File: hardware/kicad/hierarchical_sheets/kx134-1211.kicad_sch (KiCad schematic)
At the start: 0 parts

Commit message: created microcontroller schematic
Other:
- company: (none) -> Missouri S&T Rocket Design Team
- title: (none) -> SRAD-FC
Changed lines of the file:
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@@
 (kicad_sch (version 20230121) (generator eeschema)
-  (paper "A4")
+  (paper "USLetter")
+  (title_block
+    (title "SRAD-FC")
+    (company "Missouri S&T Rocket Design Team")
+  )
 )

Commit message: fixed weird fork on high g accel sheet
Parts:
- added C6, C7: 100n, symbol Device:C
- added U4: KX134-1211, Package_LGA:LGA-12_2x2mm_P0.5mm, symbol Sensor_Motion:KX122-1042
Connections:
- new net +3.3V: C6.1, C7.1, U4.3 (IO_VDD), U4.7 (VDD)
- new net GND: C6.2, C7.2, U4.8 (GND), U4.9 (GND)
- new net MISO: U4.1 (SDO/ADDR)
- new net MOSI: U4.2 (SDI/SDA)
- new net SCK: U4.12 (SCLK/SCL)
- new net ~{CS}: U4.10 (~{nCS})
- no-connect marks 0 -> 4

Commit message: massive comment upload
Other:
- note added: "Comments: - Add a ~{CS} pullup resistor between the ~{CS} pin and 3.3v. Make this resistor 10k. The only purpose of this resistor is to ensure that the chip stays inactive while the microcontroller is being initially programmed since during programming the chip will be unable to hold the various ~{CS} lines high. (The MOSI/MISO lines are used by the programmer so if this chip starts communicating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"
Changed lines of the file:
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@@
     (stroke (width 0) (type default))
+  )
+  (text "Comments:\n\n- Add a ~{CS} pullup resistor between the ~{CS} pin and 3.3v. Make this resistor\n	10k. The only purpose of this resistor is to ensure that the chip stays inactive \n	while the microcontroller is being initially programmed since during programming the chip\n	will be unable to hold the various ~{CS} lines high. (The MOSI/MISO lines \n	are used by the programmer so if this chip starts communicating while\n	the programmer is communicating to the microcontroller it could be really \n	bad.) A higher value resistor is less likely to cause problems during normal \n	operation. \n\n\n			-Seth"
+    (at 113.665 60.96 0)
+    (effects (font (size 2 2) (thickness 0.4) bold (color 255 48 0 1)) (justify left bottom))
   )
   (label "~{CS}" (at 50.8 82.55 0) (fields_autoplaced)

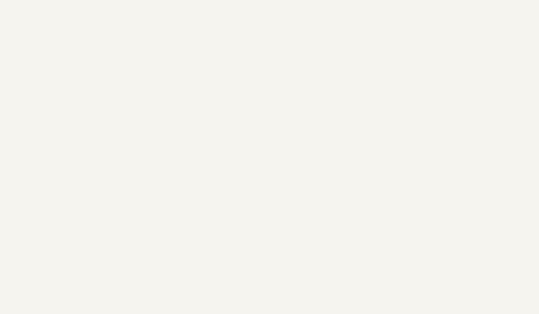
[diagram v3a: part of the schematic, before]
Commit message: added max current
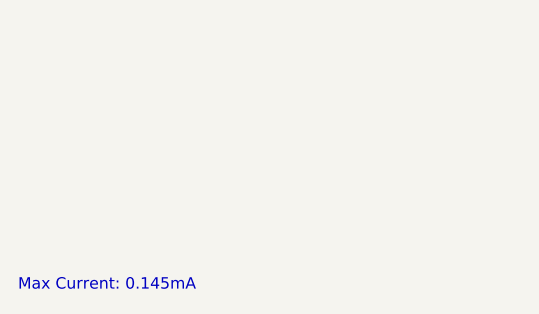
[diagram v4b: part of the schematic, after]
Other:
- note added: "Max Current: 0.145mA"
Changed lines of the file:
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@@
     (effects (font (size 2 2) (thickness 0.4) bold (color 255 48 0 1)) (justify left bottom))
+  )
+  (text "Max Current: 0.145mA" (at 13.97 201.295 0)
+    (effects (font (size 1.27 1.27)) (justify left bottom))
   )
   (label "~{CS}" (at 50.8 82.55 0) (fields_autoplaced)

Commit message: fixed schematic
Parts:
- added R23: 10k, symbol Device:R
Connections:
- net +3.3V: now also R23.1
- net ~{CS}: now also R23.2
- net INT: now reaches U4.5 (INT1)
- no-connect marks 4 -> 3
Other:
- note removed: "Comments: - Add a ~{CS} pullup resistor between the ~{CS} pin and 3.3v. Make this resistor 10k. The only purpose of this resistor is to ensure that the chip stays inactive while the microcontroller is being initially programmed since during programming the chip will be unable to hold the various ~{CS} lines high. (The MOSI/MISO lines are used by the programmer so if this chip starts communicating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"
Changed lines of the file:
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@@
   (junction (at 90.17 52.07) (diameter 0) (color 0 0 0 0)
+  )
+  (junction (at 49.53 82.55) (diameter 0) (color 0 0 0 0)
   )
   (junction (at 90.17 66.04) (diameter 0) (color 0 0 0 0)
@@
   (no_connect (at 80.01 95.25))
   (no_connect (at 80.01 87.63))
-  (no_connect (at 80.01 85.09))
   (wire (pts (xy 90.17 62.23) (xy 90.17 66.04))
+    (stroke (width 0) (type default))
+  )
+  (wire (pts (xy 49.53 82.55) (xy 49.53 76.2))
     (stroke (width 0) (type default))
   )
@@
     (stroke (width 0) (type default))
   )
-  (wire (pts (xy 67.31 74.93) (xy 67.31 67.31))
+  (wire (pts (xy 49.53 63.5) (xy 49.53 68.58))
     (stroke (width 0) (type default))
   )
-  (wire (pts (xy 45.72 82.55) (xy 57.15 82.55))
+  (wire (pts (xy 67.31 74.93) (xy 67.31 67.31))
     (stroke (width 0) (type default))
   )
@@
   )
   (wire (pts (xy 69.85 74.93) (xy 69.85 67.31))
+    (stroke (width 0) (type default))
+  )
+  (wire (pts (xy 49.53 82.55) (xy 57.15 82.55))
+    (stroke (width 0) (type default))
+  )
+  (wire (pts (xy 40.64 82.55) (xy 49.53 82.55))
     (stroke (width 0) (type default))
   )
@@
     (stroke (width 0) (type default))
   )
+  (wire (pts (xy 80.01 85.09) (xy 88.9 85.09))
+    (stroke (width 0) (type default))
+  )
   (wire (pts (xy 90.17 52.07) (xy 90.17 54.61))
     (stroke (width 0) (type default))
@@
     (stroke (width 0) (type default))
   )
-  (text "Comments:\n\n- Add a ~{CS} pullup resistor between the ~{CS} pin and 3.3v. Make this resistor\n	10k. The only purpose of this resistor is to ensure that the chip stays inactive \n	while the microcontroller is being initially programmed since during programming the chip\n	will be unable to hold the various ~{CS} lines high. (The MOSI/MISO lines \n	are used by the programmer so if this chip starts communicating while\n	the programmer is communicating to the microcontroller it could be really \n	bad.) A higher value resistor is less likely to cause problems during normal \n	operation. \n\n\n			-Seth"
-    (at 113.665 60.96 0)
-    (effects (font (size 2 2) (thickness 0.4) bold (color 255 48 0 1)) (justify left bottom))
-  )
   (text "Max Current: 0.145mA" (at 13.97 201.295 0)
     (effects (font (size 1.27 1.27)) (justify left bottom))
   )
-  (label "~{CS}" (at 50.8 82.55 0) (fields_autoplaced)
+  (label "~{CS}" (at 44.45 82.55 0) (fields_autoplaced)
+    (effects (font (size 1.27 1.27)) (justify left bottom))
+  )
+  (label "INT" (at 81.28 85.09 0) (fields_autoplaced)
     (effects (font (size 1.27 1.27)) (justify left bottom))
   )
@@
     (effects (font (size 1.27 1.27)) (justify left bottom))
   )
-  (hierarchical_label "~{CS}" (shape output) (at 45.72 82.55 180) (fields_autoplaced)
+  (hierarchical_label "~{CS}" (shape output) (at 40.64 82.55 180) (fields_autoplaced)
     (effects (font (size 1.27 1.27)) (justify right))
   )
   (hierarchical_label "MISO" (shape output) (at 45.72 87.63 180) (fields_autoplaced)
     (effects (font (size 1.27 1.27)) (justify right))
+  )
+  (hierarchical_label "INT" (shape output) (at 88.9 85.09 0) (fields_autoplaced)
+    (effects (font (size 1.27 1.27)) (justify left))
   )
   (hierarchical_label "MOSI" (shape input) (at 45.72 85.09 180) (fields_autoplaced)
@@
         )
       )
+    )
+  )
+  (symbol (lib_id "Device:R") (at 49.53 72.39 0) (unit 1)
+    (in_bom yes) (on_board yes) (dnp no) (fields_autoplaced)
+    (property "Reference" "R23" (at 52.07 71.12 0)
+      (effects (font (size 1.27 1.27)) (justify left))
+    )
+    (property "Value" "10k" (at 52.07 73.66 0)
+      (effects (font (size 1.27 1.27)) (justify left))
+    )
+    (property "Footprint" "" (at 47.752 72.39 90)
+      (effects (font (size 1.27 1.27)) hide)
+    )
+    (property "Datasheet" "~" (at 49.53 72.39 0)
+      (effects (font (size 1.27 1.27)) hide)
+    )
+    (pin "1")
+    (pin "2")
+    (instances
+      (project "FC"
+        (path "/54cce219-8b98-4e71-96c4-f9ee784aa3bc/cf41b566-7189-40a2-a24f-d689fa8a8692"
+          (reference "R23") (unit 1)
+        )
+      )
+    )
+  )
+  (symbol (lib_id "power:+3.3V") (at 49.53 63.5 0) (unit 1)
+    (in_bom yes) (on_board yes) (dnp no) (fields_autoplaced)
+    (property "Reference" "#PWR042" (at 49.53 67.31 0)
+      (effects (font (size 1.27 1.27)) hide)
+    )
+    (property "Value" "+3.3V" (at 49.53 58.42 0)
+      (effects (font (size 1.27 1.27)))
+    )
+    (property "Footprint" "" (at 49.53 63.5 0)
+      (effects (font (size 1.27 1.27)) hide)
+    )
+    (property "Datasheet" "" (at 49.53 63.5 0)
+      (effects (font (size 1.27 1.27)) hide)
+    )
+    (pin "1")
+    (instances
+      (project "FC"
+        (path "/54cce219-8b98-4e71-96c4-f9ee784aa3bc/cf41b566-7189-40a2-a24f-d689fa8a8692"
+          (reference "#PWR042") (unit 1)
+        )
+      )

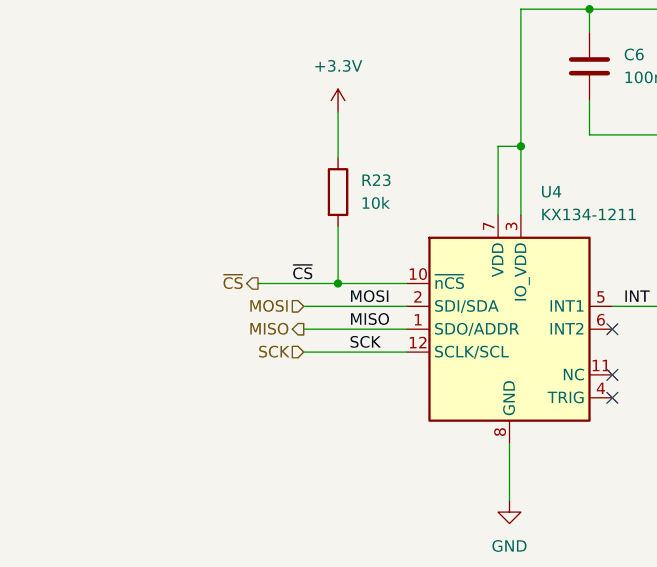
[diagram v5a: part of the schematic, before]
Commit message: started linking together FC, changed cs directions
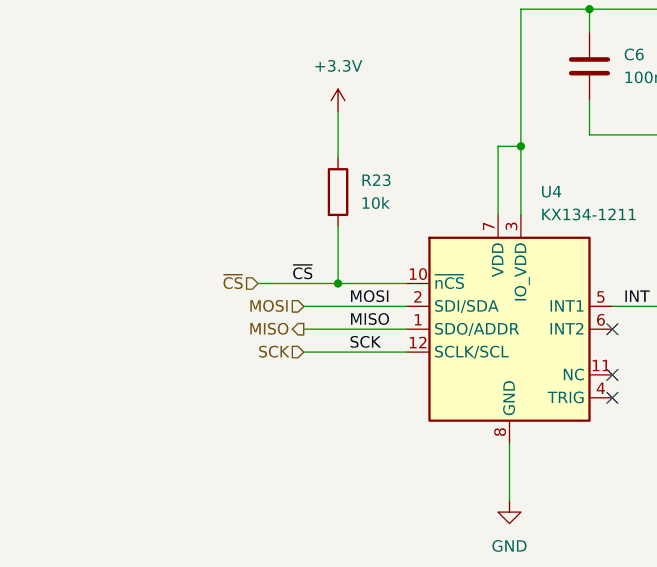
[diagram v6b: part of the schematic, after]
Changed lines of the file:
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@@
     (effects (font (size 1.27 1.27)) (justify left bottom))
   )
-  (hierarchical_label "~{CS}" (shape output) (at 40.64 82.55 180) (fields_autoplaced)
+  (hierarchical_label "~{CS}" (shape input) (at 40.64 82.55 180) (fields_autoplaced)
     (effects (font (size 1.27 1.27)) (justify right))
   )

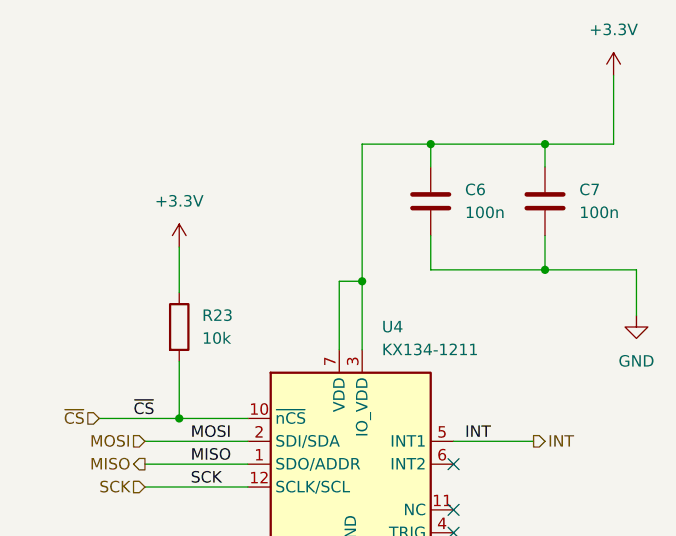
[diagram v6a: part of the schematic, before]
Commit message: assigned footprints
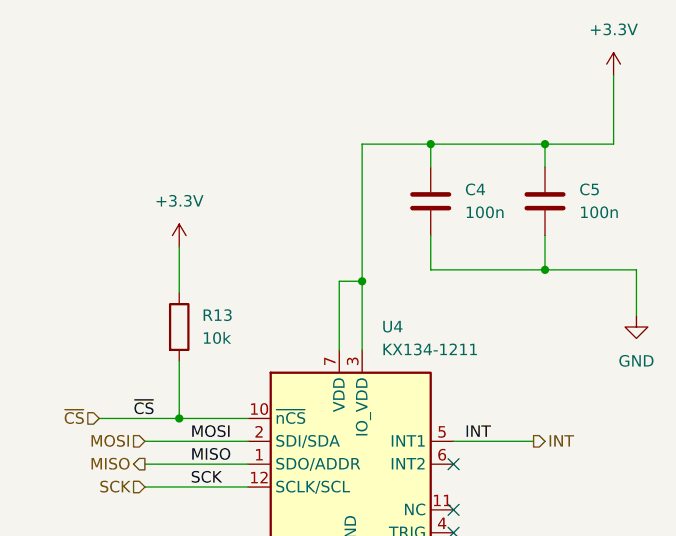
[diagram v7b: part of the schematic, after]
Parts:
- C4: renamed from C6; footprint (none) -> Resistor_SMD:R_0603_1608Metric
- C5: renamed from C7; footprint (none) -> Resistor_SMD:R_0603_1608Metric
- R13: renamed from R23; footprint (none) -> Resistor_SMD:R_0603_1608Metric
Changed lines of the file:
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@@
   (symbol (lib_id "power:+3.3V") (at 97.79 44.45 0) (unit 1)
     (in_bom yes) (on_board yes) (dnp no) (fields_autoplaced)
-    (property "Reference" "#PWR017" (at 97.79 48.26 0)
+    (property "Reference" "#PWR015" (at 97.79 48.26 0)
       (effects (font (size 1.27 1.27)) hide)
     )
@@
       (project "FC"
         (path "/54cce219-8b98-4e71-96c4-f9ee784aa3bc/cf41b566-7189-40a2-a24f-d689fa8a8692"
-          (reference "#PWR017") (unit 1)
+          (reference "#PWR015") (unit 1)
         )
       )
@@
   (symbol (lib_id "Device:R") (at 49.53 72.39 0) (unit 1)
     (in_bom yes) (on_board yes) (dnp no) (fields_autoplaced)
-    (property "Reference" "R23" (at 52.07 71.12 0)
+    (property "Reference" "R13" (at 52.07 71.12 0)
       (effects (font (size 1.27 1.27)) (justify left))
     )
@@
       (effects (font (size 1.27 1.27)) (justify left))
     )
-    (property "Footprint" "" (at 47.752 72.39 90)
+    (property "Footprint" "Resistor_SMD:R_0603_1608Metric" (at 47.752 72.39 90)
       (effects (font (size 1.27 1.27)) hide)
     )
@@
       (project "FC"
         (path "/54cce219-8b98-4e71-96c4-f9ee784aa3bc/cf41b566-7189-40a2-a24f-d689fa8a8692"
-          (reference "R23") (unit 1)
+          (reference "R13") (unit 1)
         )
       )
@@
   (symbol (lib_id "power:+3.3V") (at 49.53 63.5 0) (unit 1)
     (in_bom yes) (on_board yes) (dnp no) (fields_autoplaced)
-    (property "Reference" "#PWR042" (at 49.53 67.31 0)
+    (property "Reference" "#PWR013" (at 49.53 67.31 0)
       (effects (font (size 1.27 1.27)) hide)
     )
@@
       (project "FC"
         (path "/54cce219-8b98-4e71-96c4-f9ee784aa3bc/cf41b566-7189-40a2-a24f-d689fa8a8692"
-          (reference "#PWR042") (unit 1)
+          (reference "#PWR013") (unit 1)
         )
       )
@@
   (symbol (lib_id "power:GND") (at 100.33 71.12 0) (unit 1)
     (in_bom yes) (on_board yes) (dnp no) (fields_autoplaced)
-    (property "Reference" "#PWR09" (at 100.33 77.47 0)
+    (property "Reference" "#PWR016" (at 100.33 77.47 0)
       (effects (font (size 1.27 1.27)) hide)
     )
@@
       (project "FC"
         (path "/54cce219-8b98-4e71-96c4-f9ee784aa3bc/cf41b566-7189-40a2-a24f-d689fa8a8692"
-          (reference "#PWR09") (unit 1)
+          (reference "#PWR016") (unit 1)
         )
       )
@@
   (symbol (lib_id "Device:C") (at 90.17 58.42 0) (unit 1)
     (in_bom yes) (on_board yes) (dnp no) (fields_autoplaced)
-    (property "Reference" "C7" (at 93.98 57.15 0)
+    (property "Reference" "C5" (at 93.98 57.15 0)
       (effects (font (size 1.27 1.27)) (justify left))
     )
@@
       (effects (font (size 1.27 1.27)) (justify left))
     )
-    (property "Footprint" "" (at 91.1352 62.23 0)
+    (property "Footprint" "Resistor_SMD:R_0603_1608Metric" (at 91.1352 62.23 0)
       (effects (font (size 1.27 1.27)) hide)
     )
@@
       (project "FC"
         (path "/54cce219-8b98-4e71-96c4-f9ee784aa3bc/cf41b566-7189-40a2-a24f-d689fa8a8692"
-          (reference "C7") (unit 1)
+          (reference "C5") (unit 1)
         )
       )
@@
   (symbol (lib_id "power:GND") (at 68.58 106.68 0) (unit 1)
     (in_bom yes) (on_board yes) (dnp no) (fields_autoplaced)
-    (property "Reference" "#PWR08" (at 68.58 113.03 0)
+    (property "Reference" "#PWR014" (at 68.58 113.03 0)
       (effects (font (size 1.27 1.27)) hide)
     )
@@
       (project "FC"
         (path "/54cce219-8b98-4e71-96c4-f9ee784aa3bc/cf41b566-7189-40a2-a24f-d689fa8a8692"
-          (reference "#PWR08") (unit 1)
+          (reference "#PWR014") (unit 1)
         )
       )
@@
   (symbol (lib_id "Device:C") (at 77.47 58.42 0) (unit 1)
     (in_bom yes) (on_board yes) (dnp no) (fields_autoplaced)
-    (property "Reference" "C6" (at 81.28 57.15 0)
+    (property "Reference" "C4" (at 81.28 57.15 0)
       (effects (font (size 1.27 1.27)) (justify left))
     )
@@
       (effects (font (size 1.27 1.27)) (justify left))
     )
-    (property "Footprint" "" (at 78.4352 62.23 0)
+    (property "Footprint" "Resistor_SMD:R_0603_1608Metric" (at 78.4352 62.23 0)
       (effects (font (size 1.27 1.27)) hide)
     )
@@
       (project "FC"
         (path "/54cce219-8b98-4e71-96c4-f9ee784aa3bc/cf41b566-7189-40a2-a24f-d689fa8a8692"
-          (reference "C6") (unit 1)
+          (reference "C4") (unit 1)
         )
       )

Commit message: making formatting more consistent
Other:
- moved on the sheet: C4, C5, R13, U4
